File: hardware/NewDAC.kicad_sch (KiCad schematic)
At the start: 67 parts, among them J2 PJ-322, U4 PCM1795, U5 LM4562, U6 LM4562, U7 OPA1656, U8 OPA1656

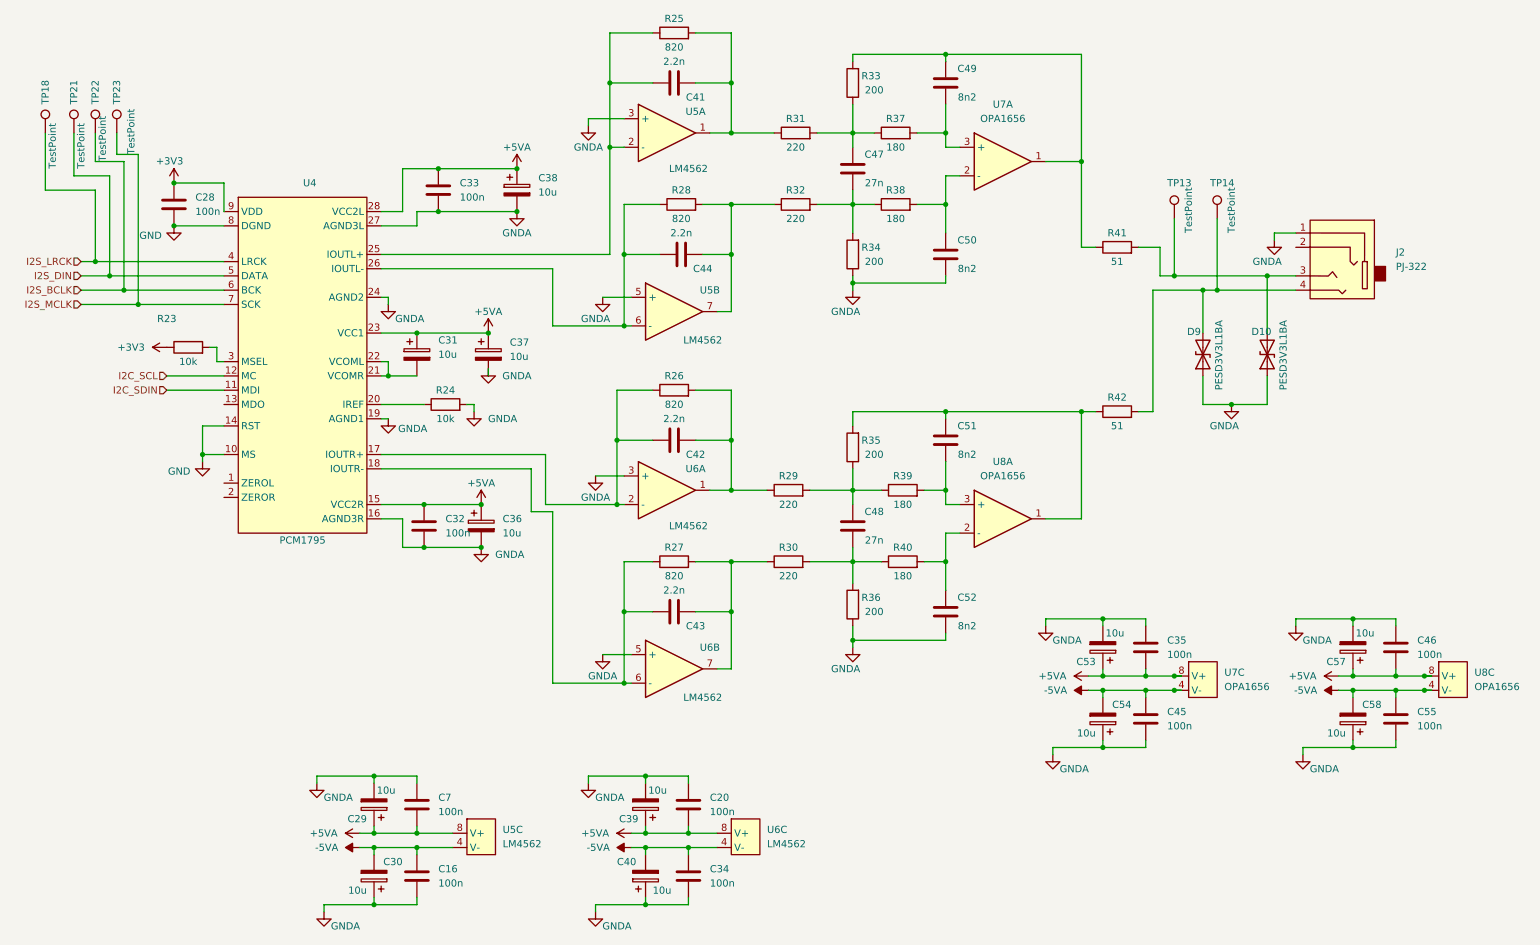
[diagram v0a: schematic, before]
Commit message: some changes on fab layers
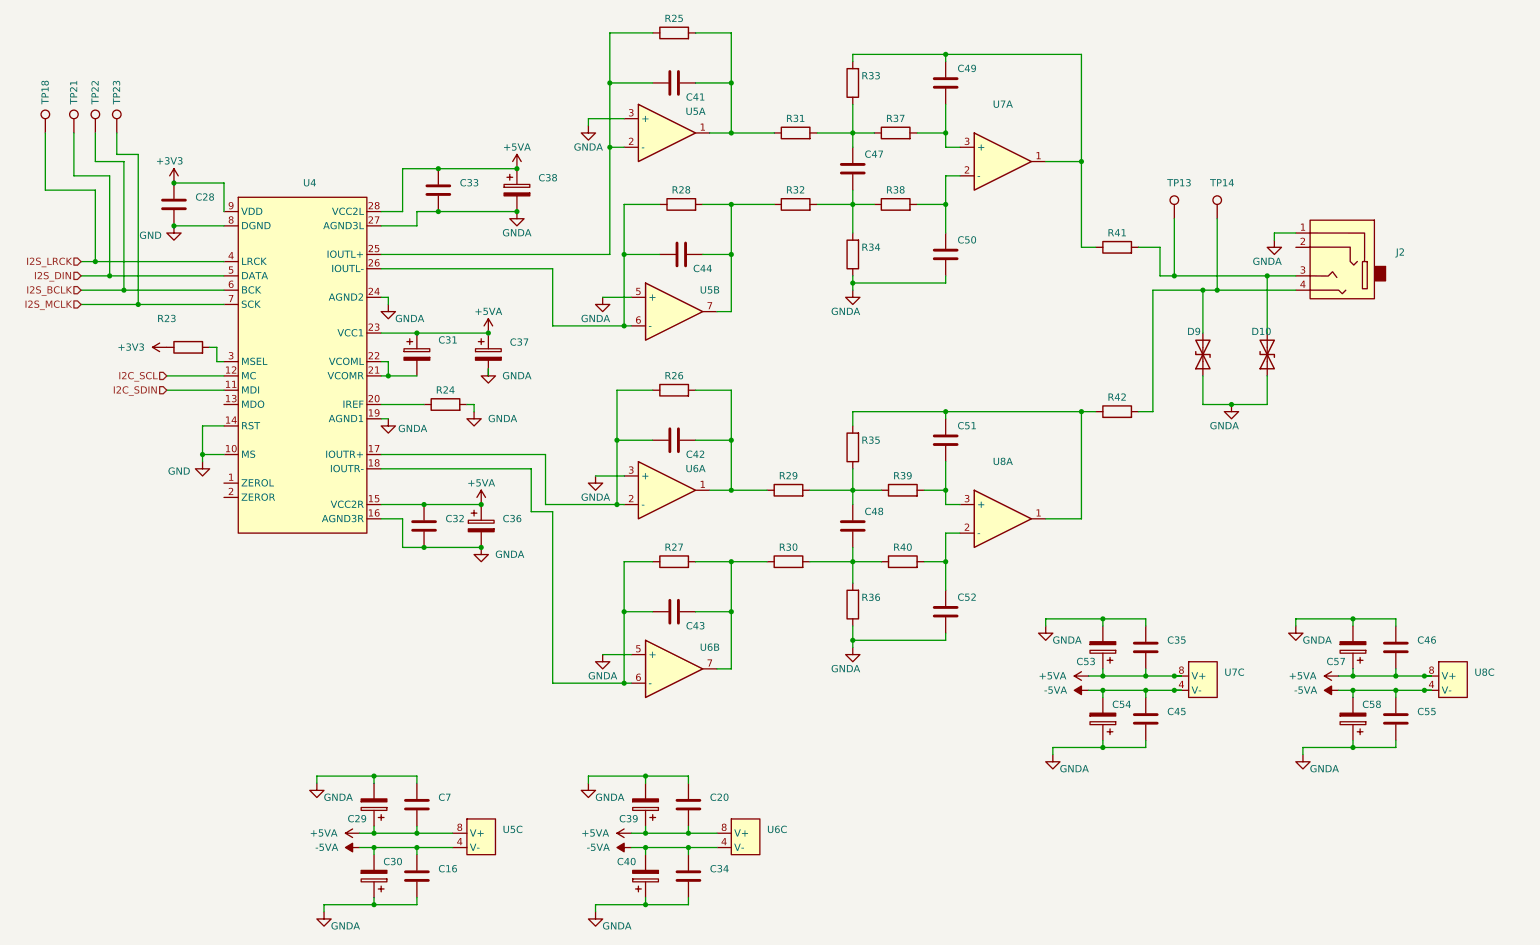
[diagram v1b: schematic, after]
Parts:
- C16, C20, C28, C32, C33, C34, C35, C45, C46, C55, C7: value 100n -> (none); footprint rlib_passive:C_0603_1608Metric -> (none)
- C29, C30, C31, C36, C37, C38, C39, C40, C53, C54, C57, C58: value 10u -> (none); footprint rlib_passive:T491A106K010AT -> (none)
- C41, C42, C43, C44: value 2.2n -> (none); footprint rlib_passive:C_0603_1608Metric -> (none)
- C47, C48: value 27n -> (none); footprint rlib_passive:C_0603_1608Metric -> (none)
- C49, C50, C51, C52: value 8n2 -> (none); footprint rlib_passive:C_0603_1608Metric -> (none)
- D10, D9: value PESD3V3L1BA -> (none); footprint rlib_passive:D_SOD-323F -> (none)
- J2: value PJ-322 -> (none); footprint rlib_connectors:PJ-322 -> (none)
- R23, R24: value 10k -> (none); footprint rlib_passive:R_0603_1608Metric -> (none)
- R25, R26, R27, R28: value 820 -> (none); footprint rlib_passive:R_0603_1608Metric -> (none)
- R29, R30, R31, R32: value 220 -> (none); footprint rlib_passive:R_0603_1608Metric -> (none)
- R33, R34, R35, R36: value 200 -> (none); footprint rlib_passive:R_0603_1608Metric -> (none)
- R37, R38, R39, R40: value 180 -> (none); footprint rlib_passive:R_0603_1608Metric -> (none)
- R41, R42: value 51 -> (none); footprint rlib_passive:R_0603_1608Metric -> (none)
- TP13, TP14, TP18, TP21, TP22, TP23: value TestPoint -> (none); footprint TestPoint:TestPoint_Pad_D1.0mm -> (none)
- U4: value PCM1795 -> (none); footprint rlib_ic:SSOP-28_5.3x10.2mm_P0.65mm -> (none)
- U5, U6: value LM4562 -> (none); footprint rlib_ic:SOIC-8_3.9x4.9mm_P1.27mm -> (none)
- U7, U8: value OPA1656 -> (none); footprint rlib_ic:SOIC-8_3.9x4.9mm_P1.27mm -> (none)

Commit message: pwr btn is optional connected to soc
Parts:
- C41, C42, C43, C44: Manufacturer YAGEO -> Murata Electronics
- C47, C48: LCSC partnumber C107086 -> C162433; Manufacturer YAGEO -> Murata Electronics; Mnfct. partnumber CC0603KRX7R9BB273 -> GRM3195C1H273JA01D
- C49, C50, C51, C52: LCSC partnumber (none) -> C97908; Manufacturer (none) -> Murata Electronics; Mnfct. partnumber (none) -> GRM2195C1H822JA01D
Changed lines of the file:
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@@
       (effects (font (size 1.27 1.27)) hide)
     )
-    (property "Manufacturer" "YAGEO" (id 7) (at 160.02 114.3 0)
-      (effects (font (size 1.27 1.27)) hide)
-    )
-    (property "Mnfct. partnumber" "CC0603KRX7R9BB273" (id 8) (at 160.02 114.3 0)
+    (property "Manufacturer" "Murata Electronics" (id 7) (at 160.02 114.3 0)
+      (effects (font (size 1.27 1.27)) hide)
+    )
+    (property "Mnfct. partnumber" "GRM3195C1H273JA01D" (id 8) (at 160.02 114.3 0)
       (effects (font (size 1.27 1.27)) hide)
     )
@@
       (effects (font (size 1.27 1.27)) hide)
     )
-    (property "LCSC partnumber" "C107086" (id 10) (at 160.02 114.3 0)
+    (property "LCSC partnumber" "C162433" (id 10) (at 160.02 114.3 0)
       (effects (font (size 1.27 1.27)) hide)
     )
@@
       (effects (font (size 1.27 1.27)) hide)
     )
-    (property "Manufacturer" "YAGEO" (id 7) (at 128.27 129.54 0)
+    (property "Manufacturer" "Murata Electronics" (id 7) (at 128.27 129.54 0)
       (effects (font (size 1.27 1.27)) hide)
     )
@@
       (effects (font (size 1.27 1.27)) hide)
     )
-    (property "Manufacturer" "YAGEO" (id 7) (at 128.27 35.56 0)
+    (property "Manufacturer" "Murata Electronics" (id 7) (at 128.27 35.56 0)
       (effects (font (size 1.27 1.27)) hide)
     )
@@
       (effects (font (size 1.27 1.27)) hide)
     )
-    (property "Manufacturer" "" (id 7) (at 176.53 35.56 0)
-      (effects (font (size 1.27 1.27)) hide)
-    )
-    (property "Mnfct. partnumber" "" (id 8) (at 176.53 35.56 0)
+    (property "Manufacturer" "Murata Electronics" (id 7) (at 176.53 35.56 0)
+      (effects (font (size 1.27 1.27)) hide)
+    )
+    (property "Mnfct. partnumber" "GRM2195C1H822JA01D" (id 8) (at 176.53 35.56 0)
       (effects (font (size 1.27 1.27)) hide)
     )
@@
     )
     (property "TC" "" (id 10) (at 176.53 35.56 0)
+      (effects (font (size 1.27 1.27)) hide)
+    )
+    (property "LCSC partnumber" " C97908" (id 11) (at 176.53 35.56 0)
       (effects (font (size 1.27 1.27)) hide)
     )
@@
       (effects (font (size 1.27 1.27)) hide)
     )
-    (property "Manufacturer" "YAGEO" (id 7) (at 160.02 50.8 0)
-      (effects (font (size 1.27 1.27)) hide)
-    )
-    (property "Mnfct. partnumber" "CC0603KRX7R9BB273" (id 8) (at 160.02 50.8 0)
+    (property "Manufacturer" "Murata Electronics" (id 7) (at 160.02 50.8 0)
+      (effects (font (size 1.27 1.27)) hide)
+    )
+    (property "Mnfct. partnumber" "GRM3195C1H273JA01D" (id 8) (at 160.02 50.8 0)
       (effects (font (size 1.27 1.27)) hide)
     )
@@
       (effects (font (size 1.27 1.27)) hide)
     )
-    (property "LCSC partnumber" "C107086" (id 10) (at 160.02 50.8 0)
+    (property "LCSC partnumber" "C162433" (id 10) (at 160.02 50.8 0)
       (effects (font (size 1.27 1.27)) hide)
     )
@@
       (effects (font (size 1.27 1.27)) hide)
     )
-    (property "Manufacturer" "" (id 7) (at 176.53 99.06 0)
-      (effects (font (size 1.27 1.27)) hide)
-    )
-    (property "Mnfct. partnumber" "" (id 8) (at 176.53 99.06 0)
+    (property "Manufacturer" "Murata Electronics" (id 7) (at 176.53 99.06 0)
+      (effects (font (size 1.27 1.27)) hide)
+    )
+    (property "Mnfct. partnumber" "GRM2195C1H822JA01D" (id 8) (at 176.53 99.06 0)
       (effects (font (size 1.27 1.27)) hide)
     )
@@
     )
     (property "TC" "" (id 10) (at 176.53 99.06 0)
+      (effects (font (size 1.27 1.27)) hide)
+    )
+    (property "LCSC partnumber" " C97908" (id 11) (at 176.53 99.06 0)
       (effects (font (size 1.27 1.27)) hide)
     )
@@
       (effects (font (size 1.27 1.27)) hide)
     )
-    (property "Manufacturer" "" (id 7) (at 176.53 66.04 0)
-      (effects (font (size 1.27 1.27)) hide)
-    )
-    (property "Mnfct. partnumber" "" (id 8) (at 176.53 66.04 0)
+    (property "Manufacturer" "Murata Electronics" (id 7) (at 176.53 66.04 0)
+      (effects (font (size 1.27 1.27)) hide)
+    )
+    (property "Mnfct. partnumber" "GRM2195C1H822JA01D" (id 8) (at 176.53 66.04 0)
       (effects (font (size 1.27 1.27)) hide)
     )
@@
     )
     (property "TC" "" (id 10) (at 176.53 66.04 0)
+      (effects (font (size 1.27 1.27)) hide)
+    )
+    (property "LCSC partnumber" " C97908" (id 11) (at 176.53 66.04 0)
       (effects (font (size 1.27 1.27)) hide)
     )
@@
       (effects (font (size 1.27 1.27)) hide)
     )
-    (property "Manufacturer" "YAGEO" (id 7) (at 128.27 99.06 0)
+    (property "Manufacturer" "Murata Electronics" (id 7) (at 128.27 99.06 0)
       (effects (font (size 1.27 1.27)) hide)
     )
@@
       (effects (font (size 1.27 1.27)) hide)
     )
-    (property "Manufacturer" "YAGEO" (id 7) (at 129.54 66.04 0)
+    (property "Manufacturer" "Murata Electronics" (id 7) (at 129.54 66.04 0)
       (effects (font (size 1.27 1.27)) hide)
     )
@@
       (effects (font (size 1.27 1.27)) hide)
     )
-    (property "Manufacturer" "" (id 7) (at 176.53 129.54 0)
-      (effects (font (size 1.27 1.27)) hide)
-    )
-    (property "Mnfct. partnumber" "" (id 8) (at 176.53 129.54 0)
+    (property "Manufacturer" "Murata Electronics" (id 7) (at 176.53 129.54 0)
+      (effects (font (size 1.27 1.27)) hide)
+    )
+    (property "Mnfct. partnumber" "GRM2195C1H822JA01D" (id 8) (at 176.53 129.54 0)
       (effects (font (size 1.27 1.27)) hide)
     )
@@
       (effects (font (size 1.27 1.27)) hide)
     )
+    (property "LCSC partnumber" " C97908" (id 11) (at 176.53 129.54 0)
+      (effects (font (size 1.27 1.27)) hide)
+    )

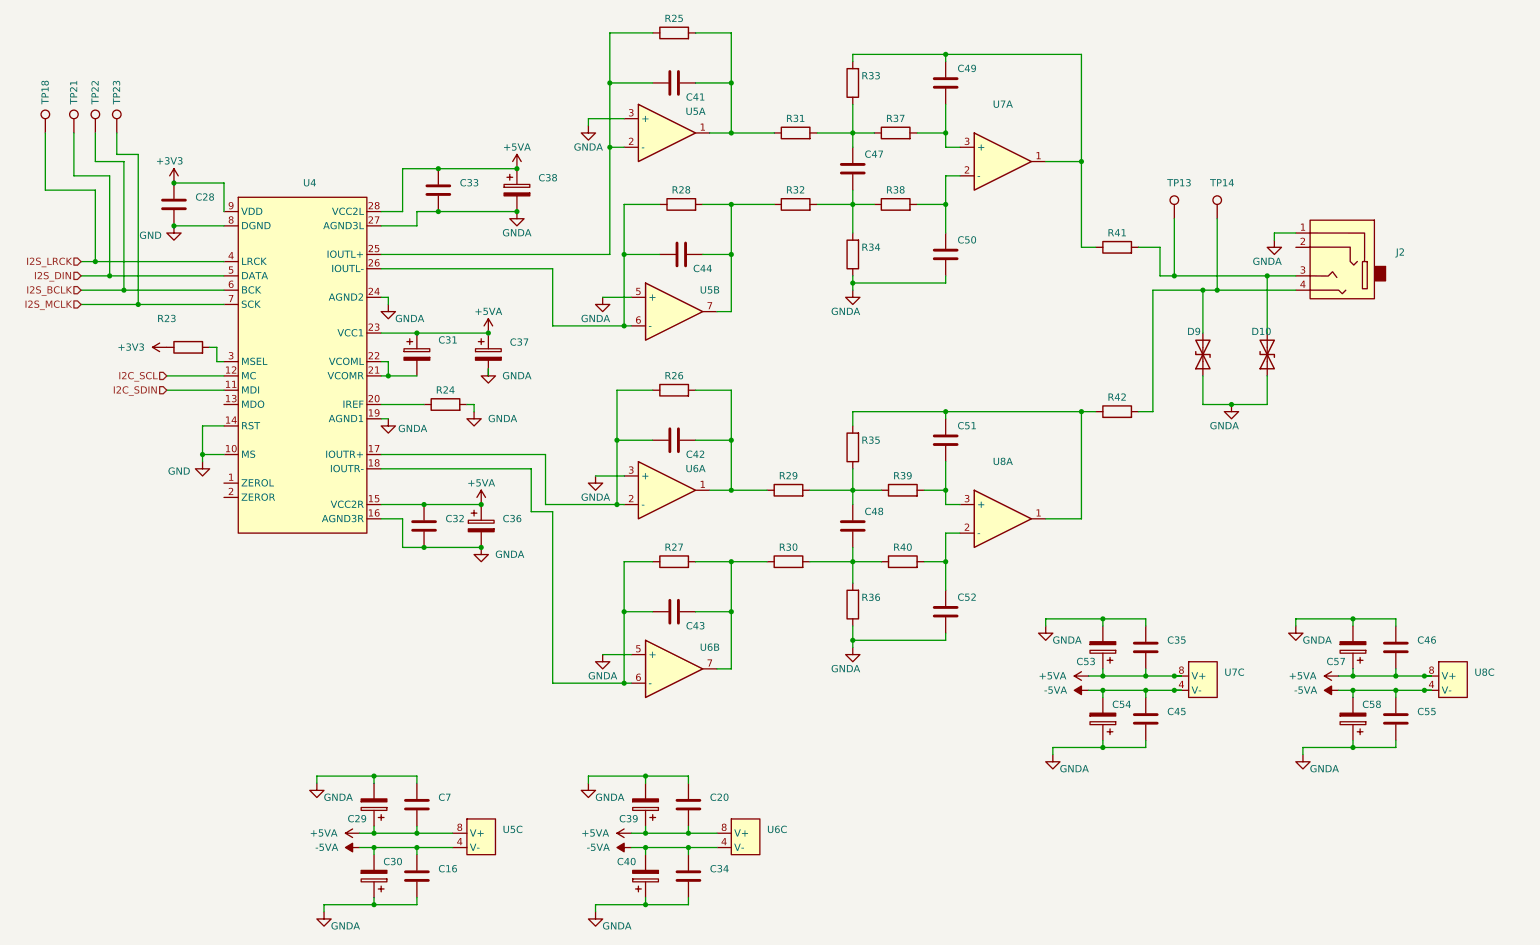
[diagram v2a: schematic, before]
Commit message: ferrite bead in adc power net is added
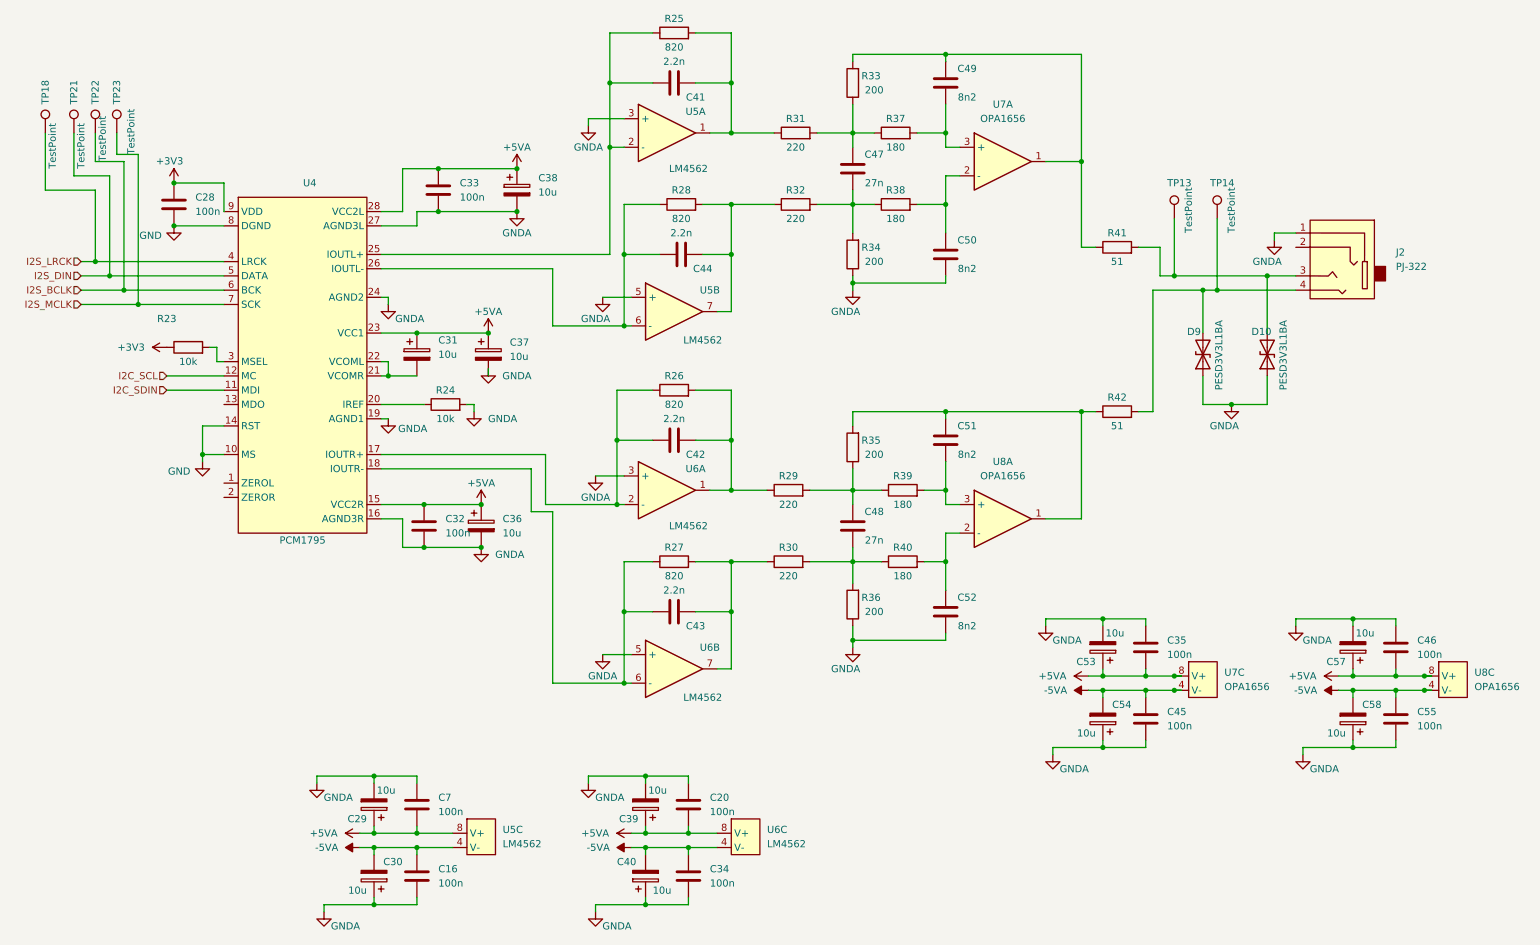
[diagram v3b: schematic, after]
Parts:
- C16, C20, C28, C32, C33, C34, C35, C45, C46, C55, C7: value (none) -> 100n; footprint (none) -> rlib_passive:C_0603_1608Metric
- C29, C30, C31, C36, C37, C38, C39, C40, C53, C54, C57, C58: value (none) -> 10u; footprint (none) -> rlib_passive:T491A106K010AT
- C41, C42, C43, C44: value (none) -> 2.2n; footprint (none) -> rlib_passive:C_0603_1608Metric
- C47, C48: value (none) -> 27n; footprint (none) -> rlib_passive:C_1206_3216Metric
- C49, C50, C51, C52: value (none) -> 8n2; footprint (none) -> rlib_passive:C_0805_2012Metric
- D10, D9: value (none) -> PESD3V3L1BA; footprint (none) -> rlib_passive:D_SOD-323F
- J2: value (none) -> PJ-322; footprint (none) -> rlib_connectors:PJ-322
- R23, R24: value (none) -> 10k; footprint (none) -> rlib_passive:R_0603_1608Metric
- R25, R26, R27, R28: value (none) -> 820; footprint (none) -> rlib_passive:R_0603_1608Metric
- R29, R30, R31, R32: value (none) -> 220; footprint (none) -> rlib_passive:R_0603_1608Metric
- R33, R34, R35, R36: value (none) -> 200; footprint (none) -> rlib_passive:R_0603_1608Metric
- R37, R38, R39, R40: value (none) -> 180; footprint (none) -> rlib_passive:R_0603_1608Metric
- R41, R42: value (none) -> 51; footprint (none) -> rlib_passive:R_0603_1608Metric
- TP13, TP14, TP18, TP21, TP22, TP23: value (none) -> TestPoint; footprint (none) -> rlib_misc:TestPoint_Pad_D1.0mm
- U4: value (none) -> PCM1795; footprint (none) -> rlib_ic:SSOP-28_5.3x10.2mm_P0.65mm
- U5, U6: value (none) -> LM4562; footprint (none) -> rlib_ic:SOIC-8_3.9x4.9mm_P1.27mm
- U7, U8: value (none) -> OPA1656; footprint (none) -> rlib_ic:SOIC-8_3.9x4.9mm_P1.27mm

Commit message: xxx
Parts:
- C31: value 10u -> (none)
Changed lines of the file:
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@@
       (effects (font (size 1.27 1.27)) (justify left))
     )
-    (property "Value" "10u" (id 1) (at 86.36 83.82 0)
+    (property "Value" "" (id 1) (at 86.36 83.82 0)
       (effects (font (size 1.27 1.27)) (justify left))
     )
